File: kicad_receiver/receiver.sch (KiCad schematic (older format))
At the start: 28 parts, among them J1 Conn_01x05_Male, J2 Conn_01x01, U1 LP2985-3.3, U2 LP2985-3.3, U3 STM32F030F4Px, U4 NRF24L01_Breakout, U5 TP4056, U6 L9110, U7 MT3608

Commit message: more stuff added
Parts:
- added C13, C15, C19, C21: 0.1uf, Capacitor_SMD:C_0603_1608Metric_Pad1.05x0.95mm_HandSolder, symbol Device:C
- added C14, C20: 10uf, Capacitor_SMD:C_0603_1608Metric_Pad1.05x0.95mm_HandSolder, symbol Device:C
- added C16, C17: 22uf, Capacitor_SMD:C_0805_2012Metric_Pad1.15x1.40mm_HandSolder, symbol Device:C
- added C18: 10uf, Capacitor_SMD:C_0805_2012Metric_Pad1.15x1.40mm_HandSolder, symbol Device:C
- added D3: SS34, Diode_SMD:D_2114_3652Metric, symbol Device:D_Schottky
- added J3, J4, J5, J6, J7: Conn_01x01, Connector_Wire:SolderWirePad_1x01_SMD_5x10mm, symbol Connector_Generic:Conn_01x01
- added L1: 22uh, Inductor_SMD:L_10.4x10.4_H4.8, symbol Device:L
- added R10, R11: ?, Resistor_SMD:R_0603_1608Metric_Pad1.05x0.95mm_HandSolder, symbol Device:R
- added R12, R13, R6, R7: 10k, Resistor_SMD:R_0603_1608Metric_Pad1.05x0.95mm_HandSolder, symbol Device:R
- added R14, R15, R8, R9: 220, Resistor_SMD:R_0603_1608Metric_Pad1.05x0.95mm_HandSolder, symbol Device:R
- added U10: L9110, lib:L9110, symbol L9110:L9110
- added U11, U12, U8, U9: 4N26, Package_DIP:DIP-6_W7.62mm_SMDSocket_SmallPads, symbol Isolator:4N26
- C1, C10, C11, C12, C2, C8, C9: value 10мкф -> 10uf
- C3, C4, C7: value 0.1мкф -> 0.1uf
- C5, C6: value 0.01мкф -> 0.01uf
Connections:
- net BAT+: now also U7.4 (EN), U7.5 (VIN), C16.1, J7.1 (Pin_1), L1.1
- net GND: now also U5.9 (PP), U6.5 (GND), U6.8 (GND), U7.2 (GND), C14.2, C15.2, C16.2, C17.2, C18.2, C20.2, C21.2, R11.1, R14.2, R15.2, R8.2, R9.2, U10.5 (GND), U10.8 (GND), U11.4, U12.4, U8.4, U9.4
- net at C11.1, R3.2, R4.2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: no longer U5.9 (PP)
- net at U6.1 (OA): now also C13.1, J3.1 (Pin_1)
- net Vconv: now reaches U6.2 (VCC)
- net Vconv: now also U6.3 (VCC), C14.1, C15.1, C17.1, C18.1, C20.1, C21.1, D3.1 (K), R10.2, R12.1, R13.1, R6.1, R7.1, U10.2 (VCC), U10.3 (VCC)
- net at U6.4 (OB): now also C13.2, J4.1 (Pin_1)
- net at U6.6 (IA): now also R7.2, U9.5
- net at U6.7 (IB): now also R6.2, U8.5
- net at U7.1 (SW): now also D3.2 (A), L1.2
- net at U7.3 (FB): now also R10.1, R11.2
- net TIM1CH2 renamed FF_PWM
- net FF_PWM: now also U11.1, U8.1
- net TIM3CH4 renamed FB_PWM
- net FB_PWM: now also U12.1, U9.1
- new net: C19.1, J5.1 (Pin_1), U10.1 (OA)
- new net: C19.2, J6.1 (Pin_1), U10.4 (OB)
- new net: R13.2, U10.6 (IA), U12.5
- new net: R12.2, U10.7 (IB), U11.5
- new net: R14.1, U11.2
- new net: R15.1, U12.2
- new net: R8.1, U8.2
- new net: R9.1, U9.2
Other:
- moved on the sheet: C10, C11, C12, C2, C3, C4, C6, C7, C9, D1, D2, J1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

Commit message: refactored
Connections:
- net FB_PWM: no longer U12.1
- net FF_PWM: no longer U11.1
- new net TURN_LEFT: U11.1
- new net TURN_RIGHT: U12.1
- no-connect marks 0 -> 11
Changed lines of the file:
@@
 	3050 2750 3300 2750
 Wire Wire Line
-	1500 3250 1250 3250
-Wire Wire Line
-	1250 3250 1250 4200
-Wire Wire Line
-	1250 4200 3100 4200
-Wire Wire Line
-	3100 4200 3100 3150
-Wire Wire Line
-	3100 3150 3300 3150
-Wire Wire Line
-	1500 3350 1350 3350
-Wire Wire Line
-	1350 3350 1350 4300
-Wire Wire Line
 	1350 4300 3200 4300
 Wire Wire Line
 	3200 4300 3200 2950
-Wire Wire Line
-	3200 2950 3300 2950
 Text GLabel 9950 5300 2    50   Output ~ 0
 BAT+
@@
 FF_PWM
 Wire Wire Line
-	2500 3350 3000 3350
-Wire Wire Line
-	3000 3350 3000 3250
-Wire Wire Line
 	3000 3250 3300 3250
 Text GLabel 1100 3550 0    50   Output ~ 0
@@
 Connection ~ 8650 1100
 Wire Wire Line
-	7100 1850 7000 1850
-Wire Wire Line
 	7000 1850 7000 1750
 Wire Wire Line
@@
 Connection ~ 8650 3100
 Wire Wire Line
-	7100 3850 7000 3850
-Wire Wire Line
 	7000 3850 7000 3750
 Wire Wire Line
@@
 $EndComp
 Text GLabel 9900 3250 0    50   Input ~ 0
-FF_PWM
+TURN_LEFT
 Text GLabel 9900 4100 0    50   Input ~ 0
-FB_PWM
+TURN_RIGHT
 $Comp
 L Device:D_Schottky D3
@@
 Wire Wire Line
 	3400 6000 3400 5650
+NoConn ~ 10500 1250
+NoConn ~ 10500 2100
+NoConn ~ 10500 3250
+NoConn ~ 10500 4100
+NoConn ~ 3200 5900
+Wire Wire Line
+	3300 2950 3200 2950
+Wire Wire Line
+	1350 3350 1350 4300
+Wire Wire Line
+	1500 3350 1350 3350
+Wire Wire Line
+	3000 3350 3000 3250
+Wire Wire Line
+	2500 3350 3000 3350
+Wire Wire Line
+	3300 3150 3100 3150
+Wire Wire Line
+	3100 3150 3100 4200
+Wire Wire Line
+	3100 4200 1400 4200
+Wire Wire Line
+	1400 4200 1400 3250
+Wire Wire Line
+	1400 3250 1500 3250
+NoConn ~ 2500 2450
+NoConn ~ 2500 2550
+NoConn ~ 2500 2650
+NoConn ~ 2500 2750
+NoConn ~ 2500 2850
+NoConn ~ 1500 2650
+Wire Wire Line
+	7100 1850 7000 1850
+Wire Wire Line
+	7100 3850 7000 3850
 $EndSCHEMATC

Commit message: refactored
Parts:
- removed C20: 10uf, Capacitor_SMD:C_0603_1608Metric_Pad1.05x0.95mm_HandSolder, symbol Device:C
- removed C21: 0.1uf, Capacitor_SMD:C_0603_1608Metric_Pad1.05x0.95mm_HandSolder, symbol Device:C
- R10: value ? -> 88K
- R11: value ? -> 12K
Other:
- moved on the sheet: C11, C12, C19, D1, D2, J2, J7, R1, R12, R13, R14, R15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

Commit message: place done
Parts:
- removed C16, C17: 22uf, Capacitor_SMD:C_0805_2012Metric_Pad1.15x1.40mm_HandSolder, symbol Device:C
- removed C18: 10uf, Capacitor_SMD:C_0805_2012Metric_Pad1.15x1.40mm_HandSolder, symbol Device:C
- removed D3: SS34, Diode_SMD:D_2114_3652Metric, symbol Device:D_Schottky
- removed L1: 22uh, Inductor_SMD:L_10.4x10.4_H4.8, symbol Device:L
- removed R10: 88K, Resistor_SMD:R_0603_1608Metric_Pad1.05x0.95mm_HandSolder, symbol Device:R
- removed R11: 12K, Resistor_SMD:R_0603_1608Metric_Pad1.05x0.95mm_HandSolder, symbol Device:R
- removed U7: MT3608, Package_TO_SOT_SMD:SOT-23-6_Handsoldering, symbol mt3608:MT3608
- added J8: BAT+, TestPoint:TestPoint_Pad_4.0x4.0mm, symbol Connector_Generic:Conn_01x01
- added J9: BAT-, TestPoint:TestPoint_Pad_4.0x4.0mm, symbol Connector_Generic:Conn_01x01
- J2: value Conn_01x01 -> CHG+5V; footprint Connector_Wire:SolderWirePad_1x01_SMD_5x10mm -> TestPoint:TestPoint_Pad_4.0x4.0mm
- J3: value Conn_01x01 -> M1+; footprint Connector_Wire:SolderWirePad_1x01_SMD_5x10mm -> TestPoint:TestPoint_Pad_4.0x4.0mm
- J4: value Conn_01x01 -> M1-; footprint Connector_Wire:SolderWirePad_1x01_SMD_5x10mm -> TestPoint:TestPoint_Pad_4.0x4.0mm
- J5: value Conn_01x01 -> M2+; footprint Connector_Wire:SolderWirePad_1x01_SMD_5x10mm -> TestPoint:TestPoint_Pad_4.0x4.0mm
- J6: value Conn_01x01 -> M2-; footprint Connector_Wire:SolderWirePad_1x01_SMD_5x10mm -> TestPoint:TestPoint_Pad_4.0x4.0mm
- J7: value Conn_01x01 -> CHG-; footprint Connector_Wire:SolderWirePad_1x01_SMD_5x10mm -> TestPoint:TestPoint_Pad_4.0x4.0mm
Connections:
- net Vconv is gone; now on net BAT+: C14.1, C15.1, R12.1, R13.1, R6.1, R7.1, U10.2 (VCC), U10.3 (VCC), U6.2 (VCC), U6.3 (VCC)
- net BAT+: now also J8.1 (Pin_1); no longer J7.1 (Pin_1)
- net GND: now also J7.1 (Pin_1), U3.1 (BOOT0), J9.1 (Pin_1)
- net TURN_LEFT: now also U3.9 (PA3)
- net TURN_RIGHT: now also U3.10 (PA4)
- net at U4.3 (CE): now also U3.7 (PA1); no longer U3.2 (PF0)
- net at U4.4 (~CSN): now also U3.6 (PA0); no longer U3.3 (PF1)
- net at U4.8 (IRQ): now also U3.8 (PA2); no longer U3.18 (PA10)
- net +5V: no longer names the net of D1.2 (A), D2.2 (A), J2.1 (Pin_1), R3.1, R4.1
- no-connect marks 11 -> 7
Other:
- moved on the sheet: R3, R4

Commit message: fixed
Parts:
- C1, C11, C12, C13, C14, C15, C19, C2, C4, C5, C6, C7, C8, C9: footprint Capacitor_SMD:C_0603_1608Metric_Pad1.05x0.95mm_HandSolder -> Capacitor_SMD:C_0805_2012Metric_Pad1.15x1.40mm_HandSolder
- J2, J3, J4, J5, J6, J7, J8, J9: footprint TestPoint:TestPoint_Pad_4.0x4.0mm -> TestPoint:TestPoint_Pad_2.5x2.5mm
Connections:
- net NRF_CE: now reaches U4.3 (CE)
- net NRF_CE: now also U3.6 (PA0); no longer U3.7 (PA1)
- net NRF_CSN: now reaches U4.4 (~CSN)
- net NRF_CSN: now also U3.7 (PA1); no longer U3.6 (PA0)
- net SPI_SCK: now reaches U3.11 (PA5), U4.5 (SCK)
- net SPI_MOSI: now reaches U3.13 (PA7), U4.6 (MOSI)
- net SPI_MISO: now reaches U3.12 (PA6), U4.7 (MISO)
- net at U3.8 (PA2): no longer U4.8 (IRQ)
- net NRF_IRQ: now reaches U3.18 (PA10)
- net NRF_IRQ: now also U4.8 (IRQ)
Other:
- moved on the sheet: U4

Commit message: refactored
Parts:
- renumbered C9 to C10, C13 to C11, C19 to C12, C14 to C13, C15 to C14, C11 to C15, C12 to C16, C3 to C2, C4 to C3, C5 to C4, C7 to C5, C8 to C6, C10 to C7, C2 to C8, C6 to C9, J3 to J2, J4 to J3, J5 to J4, J6 to J5, J2 to J6, R8 to R10, R9 to R11, R14 to R12, R15 to R13, R3 to R2, R4 to R3, R2 to R4, R6 to R5, R12 to R6, R13 to R8, R5 to R9, U11 to U10, U12 to U11, U3 to U2, U4 to U3, U2 to U4, U6 to U5, U10 to U6, U5 to U7

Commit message: done!
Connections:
- net 3v3mcu: now also J1.1 (Pin_1); no longer J1.2 (Pin_2)
- net GND: now also J1.4 (Pin_4); no longer J1.1 (Pin_1)
- net NRF_IRQ: now also U2.8 (PA2); no longer U2.18 (PA10)
- net SWCLK: now also J1.2 (Pin_2); no longer J1.4 (Pin_4)
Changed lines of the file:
@@
 Text GLabel 5500 2500 2    50   Output ~ 0
 RST
-Text GLabel 5500 2400 2    50   Output ~ 0
+Text GLabel 5500 2200 2    50   Output ~ 0
 SWCLK
 Wire Wire Line
@@
 Text GLabel 2650 3550 2    50   Input ~ 0
 SWCLK
-Text GLabel 5500 2200 2    50   Output ~ 0
+Text GLabel 5500 2100 2    50   Output ~ 0
 3v3mcu
-Text GLabel 5500 2100 2    50   Output ~ 0
+Text GLabel 5500 2400 2    50   Output ~ 0
 GND
 Wire Wire Line
@@
 Wire Wire Line
 	3700 3700 3750 3700
-NoConn ~ 2500 2650
+NoConn ~ 2500 3350
 Wire Wire Line
 	4000 1400 4700 1400
@@
 Text GLabel 3750 3800 0    50   Output ~ 0
 NRF_IRQ
-Text GLabel 2500 3350 2    50   Output ~ 0
+Text GLabel 2500 2650 2    50   Output ~ 0
 NRF_IRQ
 Text GLabel 2500 2450 2    50   Output ~ 0

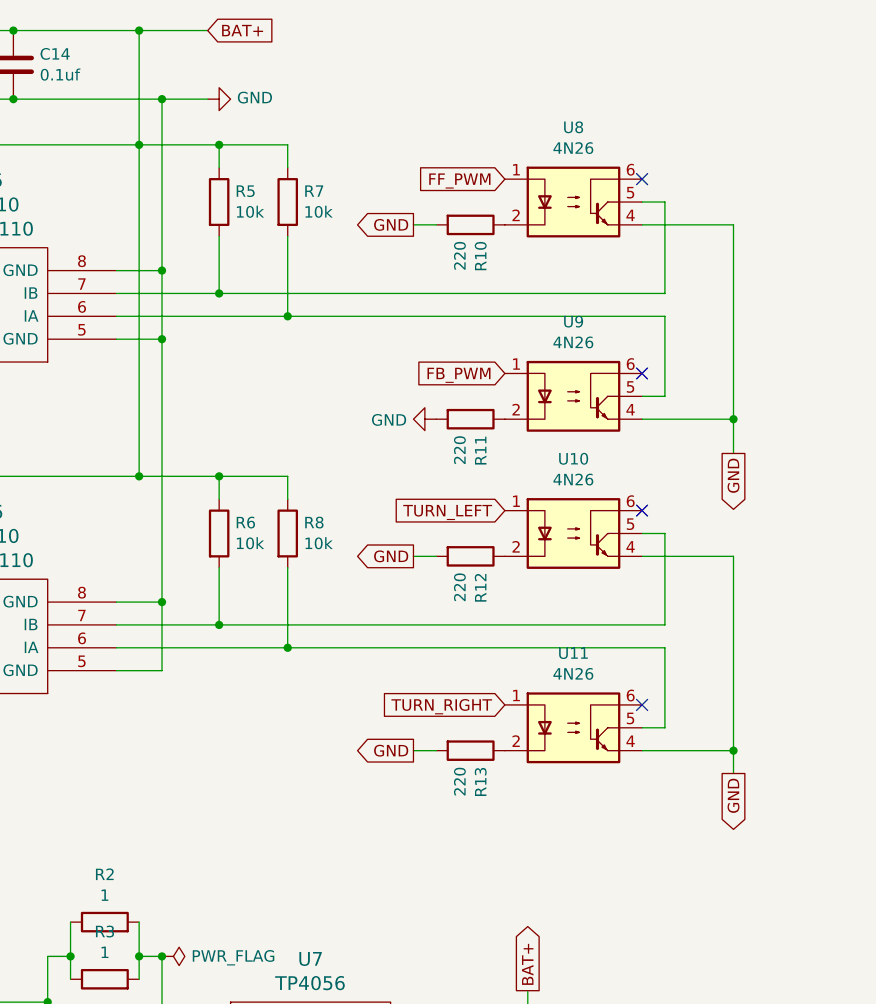
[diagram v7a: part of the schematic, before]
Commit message: optocouples removed
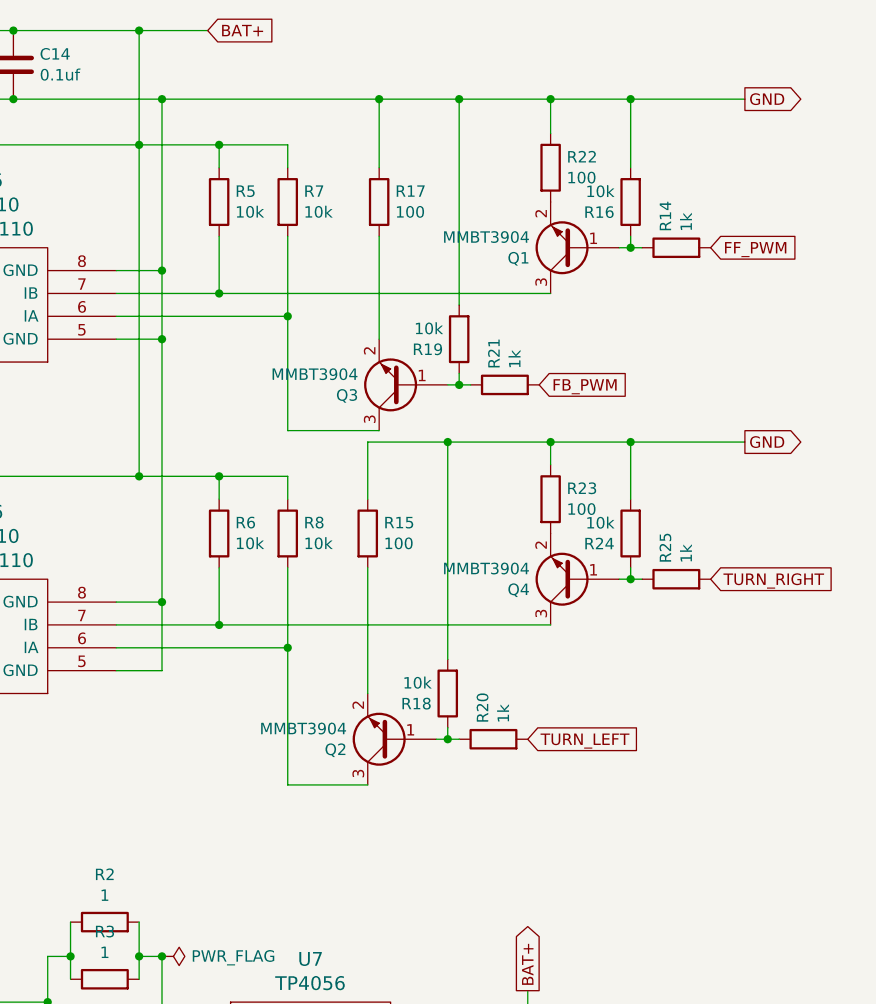
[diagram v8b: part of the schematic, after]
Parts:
- removed R10, R11, R12, R13: 220, Resistor_SMD:R_0603_1608Metric_Pad1.05x0.95mm_HandSolder, symbol Device:R
- removed U10, U11, U8, U9: 4N26, Package_DIP:DIP-6_W7.62mm_SMDSocket_SmallPads, symbol Isolator:4N26
- added Q1, Q2, Q3, Q4: MMBT3904, Package_TO_SOT_SMD:SOT-23, symbol Transistor_BJT:MMBT3904
- added R14, R20, R21, R25: 1k, Resistor_SMD:R_0603_1608Metric_Pad1.05x0.95mm_HandSolder, symbol Device:R
- added R15, R17, R22, R23: 100, Resistor_SMD:R_0603_1608Metric_Pad1.05x0.95mm_HandSolder, symbol Device:R
- added R16, R18, R19, R24: 10k, Resistor_SMD:R_0603_1608Metric_Pad1.05x0.95mm_HandSolder, symbol Device:R
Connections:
- net FB_PWM: now also R21.2
- net FF_PWM: now also R14.2
- net GND: now also R15.1, R16.2, R17.1, R18.2, R19.2, R22.1, R23.1, R24.2
- net TURN_LEFT: now also R20.2
- net TURN_RIGHT: now also R25.2
- net at R7.2, U5.6 (IA): now also Q3.3 (C)
- net at R5.2, U5.7 (IB): now also Q1.3 (C)
- net at R8.2, U6.6 (IA): now also Q2.3 (C)
- net at R6.2, U6.7 (IB): now also Q4.3 (C)
- new net: Q1.1 (B), R14.1, R16.1
- new net: Q1.2 (E), R22.2
- new net: Q3.1 (B), R19.1, R21.1
- new net: Q3.2 (E), R17.2
- new net: Q4.1 (B), R24.1, R25.1
- new net: Q4.2 (E), R23.2
- new net: Q2.1 (B), R18.1, R20.1
- new net: Q2.2 (E), R15.2
- no-connect marks 7 -> 3
